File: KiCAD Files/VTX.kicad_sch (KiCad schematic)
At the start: 33 parts, among them J2 XT90PW-M, U1 LM76003RNPR, U2 LM76003RNPR

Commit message: USB Controller Ready
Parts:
- removed C1, C10: 470n, Footprints:C0805X474K101T, symbol C0805X474K101T:C0805X475K025T
- removed C11, C7: 1u, Footprints:CC0603KRX5R6BB105, symbol CL10A474KB8NNNC:CL10A474KB8NNNC
- removed C12, C2: 2.2uF, Footprints:CC0805KKX7R6BB225, symbol CC0805KKX7R6BB225:CC0805KKX7R6BB225
- removed C13, C3: 2.2uF, Footprints:CS1005X7R474K6R3NR, symbol CS1005X7R474K6R3NR:CC0805KKX7R6BB225
- removed C14, C6: 10p, Footprints:10pF16V, symbol 10pF16V:08051A100FAT2A
- removed C15, C8: 68u, Footprints:RR71C680MDN1, symbol RR71C680MDN1:RR71C680MDN1KX
- removed C16, C5: 470n, Footprints:CL10A474KB8NNNC, symbol CL10A474KB8NNNC:CL10A474KB8NNNC
- removed C4, C9: 4.7u, Footprints:CS3225X7R475K101NRK, symbol CS3225X7R475K101NRK:C1210C475K3PACTU
- removed L1, L2: 6060_78439346150, Footprints:L78439346150, symbol 78439346150:6060_78439346150
- removed R1, R5: 105K, Footprints:RC1206FR-07105KL, symbol RC1206FR-07105KL:RC1206FR-07105KL
- removed R2, R7: 24K9, Footprints:AC0402FR-0724K9L, symbol AC0402FR-0724K9L:AC0402FR-0724K9L
- removed R3, R4, R6, R8: 100K, Footprints:RC0402FR-07100KL, symbol RC0402FR-07100KL:RC0402FR-07100KL
- removed U1, U2: LM76003RNPR, Footprints:LM76003RNPR, symbol LM76003RNPR:LM76003RNPR
- added J1: Conn_02x20_Odd_Even, Connector_PinHeader_2.54mm:PinHeader_2x20_P2.54mm_Vertical, symbol Connector_Generic:Conn_02x20_Odd_Even
- added U1: BL-M8812EU2, Package_DFN_QFN:Texas_RVA_VQFN-16-1EP_3.5x3.5mm_P0.5mm_EP2.14x2.14mm_ThermalVias, symbol BL-M8812EU2:BL-M8812EU2
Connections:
- net GND: now also J1.14 (Pin_14), J1.20 (Pin_20), J1.25 (Pin_25), J1.30 (Pin_30), J1.34 (Pin_34), J1.39 (Pin_39), J1.6 (Pin_6), J1.9 (Pin_9), U1.1 (GND), U1.10 (GND), U1.11 (GND), U1.12 (GND), U1.13 (GND), U1.14 (GND), U1.15 (GND), U1.16 (GND), U1.17 (GND), U1.18 (GND), U1.19 (GND), U1.20 (GND), U1.21 (GND), U1.22 (GND), U1.23 (GND), U1.24 (GND), U1.25 (GND), U1.26 (GND), U1.27 (GND), U1.28 (GND), U1.29 (GND), U1.30 (GND), U1.31 (GND), U1.32 (GND), U1.33 (GND), U1.34 (GND), U1.35 (GND), U1.36 (GND), U1.37 (GND), U1.38 (GND), U1.4 (GND), U1.8 (GND), U1.9 (GND)
- new net +5V_Radxa: J1.2 (Pin_2), J1.4 (Pin_4)
- new net +5V_WiFi: U1.6 (VDD5.0), U1.7 (VDD5.0)
- new net USB Hub/USBDM_DN1: U1.3 (USB2.0-DM)
- new net USB Hub/USBDP_DN1: U1.2 (USB2.0+DP)
- new net USBDM_UP: J1.28 (Pin_28)
- new net USBDP_UP: J1.27 (Pin_27)
- no-connect marks 2 -> 1
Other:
- added sheet Buck Converter (buck_converter.kicad_sch)
- added sheet USB Hub (usb_hub.kicad_sch)
- note added: "BL-M8812EU2"
- note added: "Mounting Holes"
- note added: "Radxa ZERO 3W"
- note removed: "Buck Converter 1"
- note removed: "Buck Converter 2"
- moved on the sheet: H1, H2, H3, H4, J2

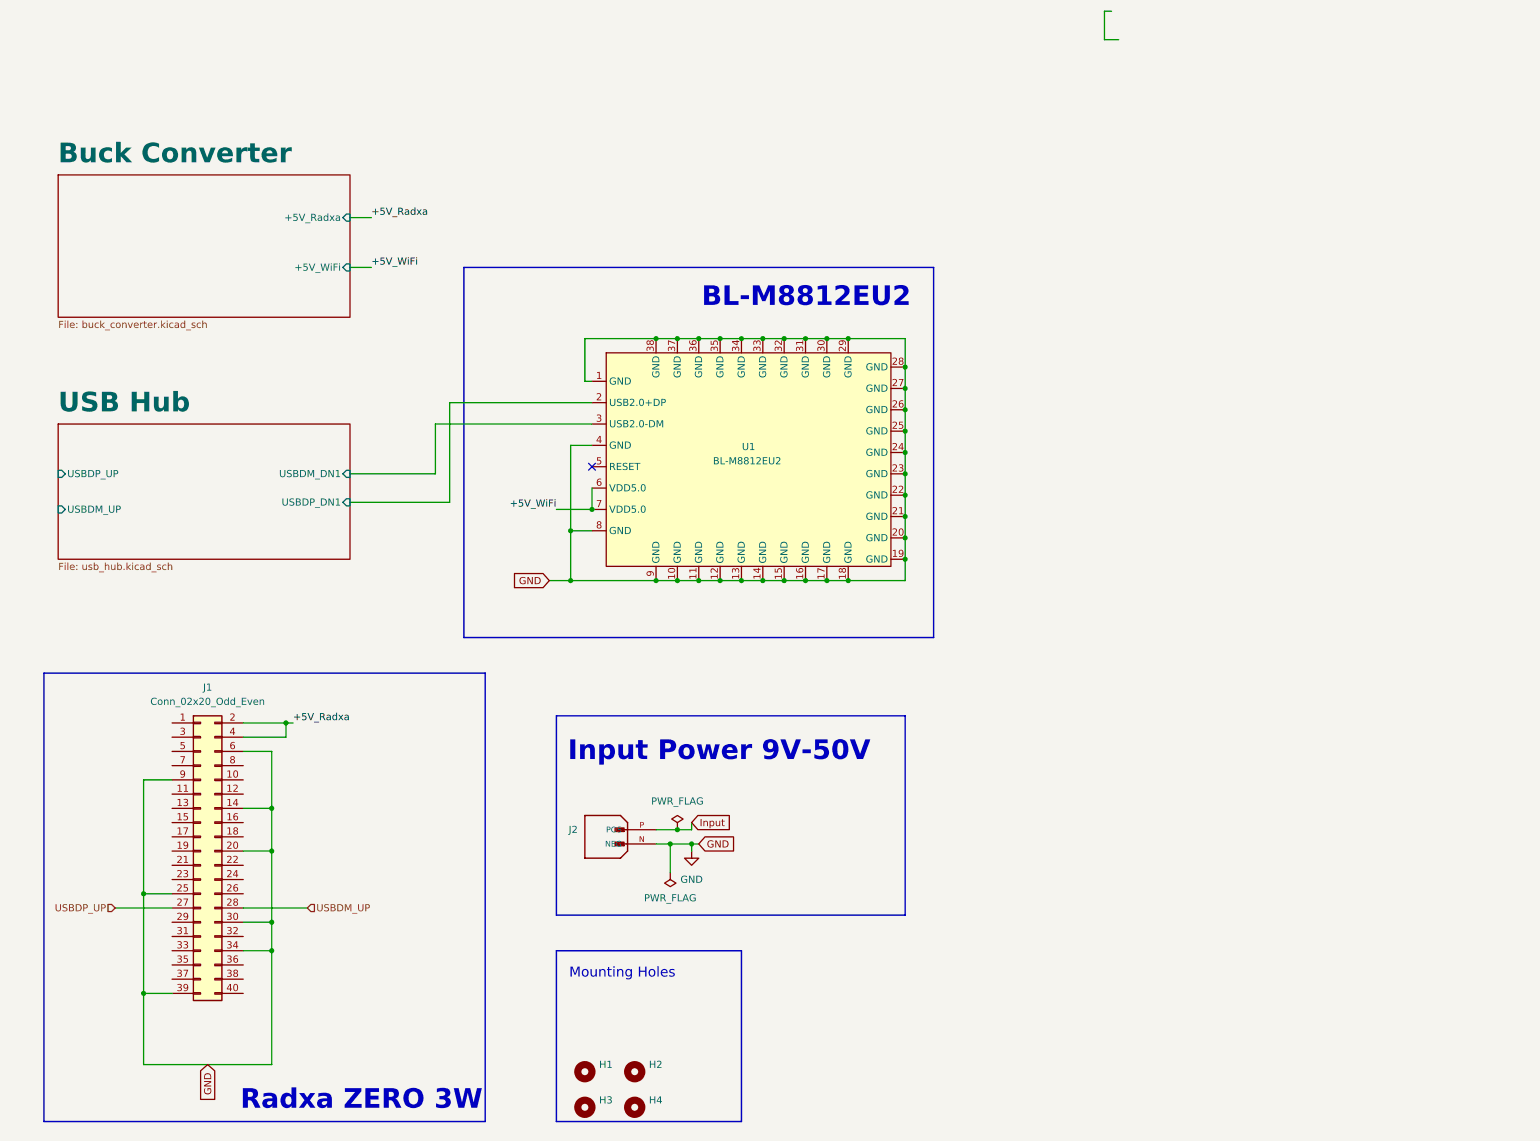
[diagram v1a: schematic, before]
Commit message: Ethernet routing pending
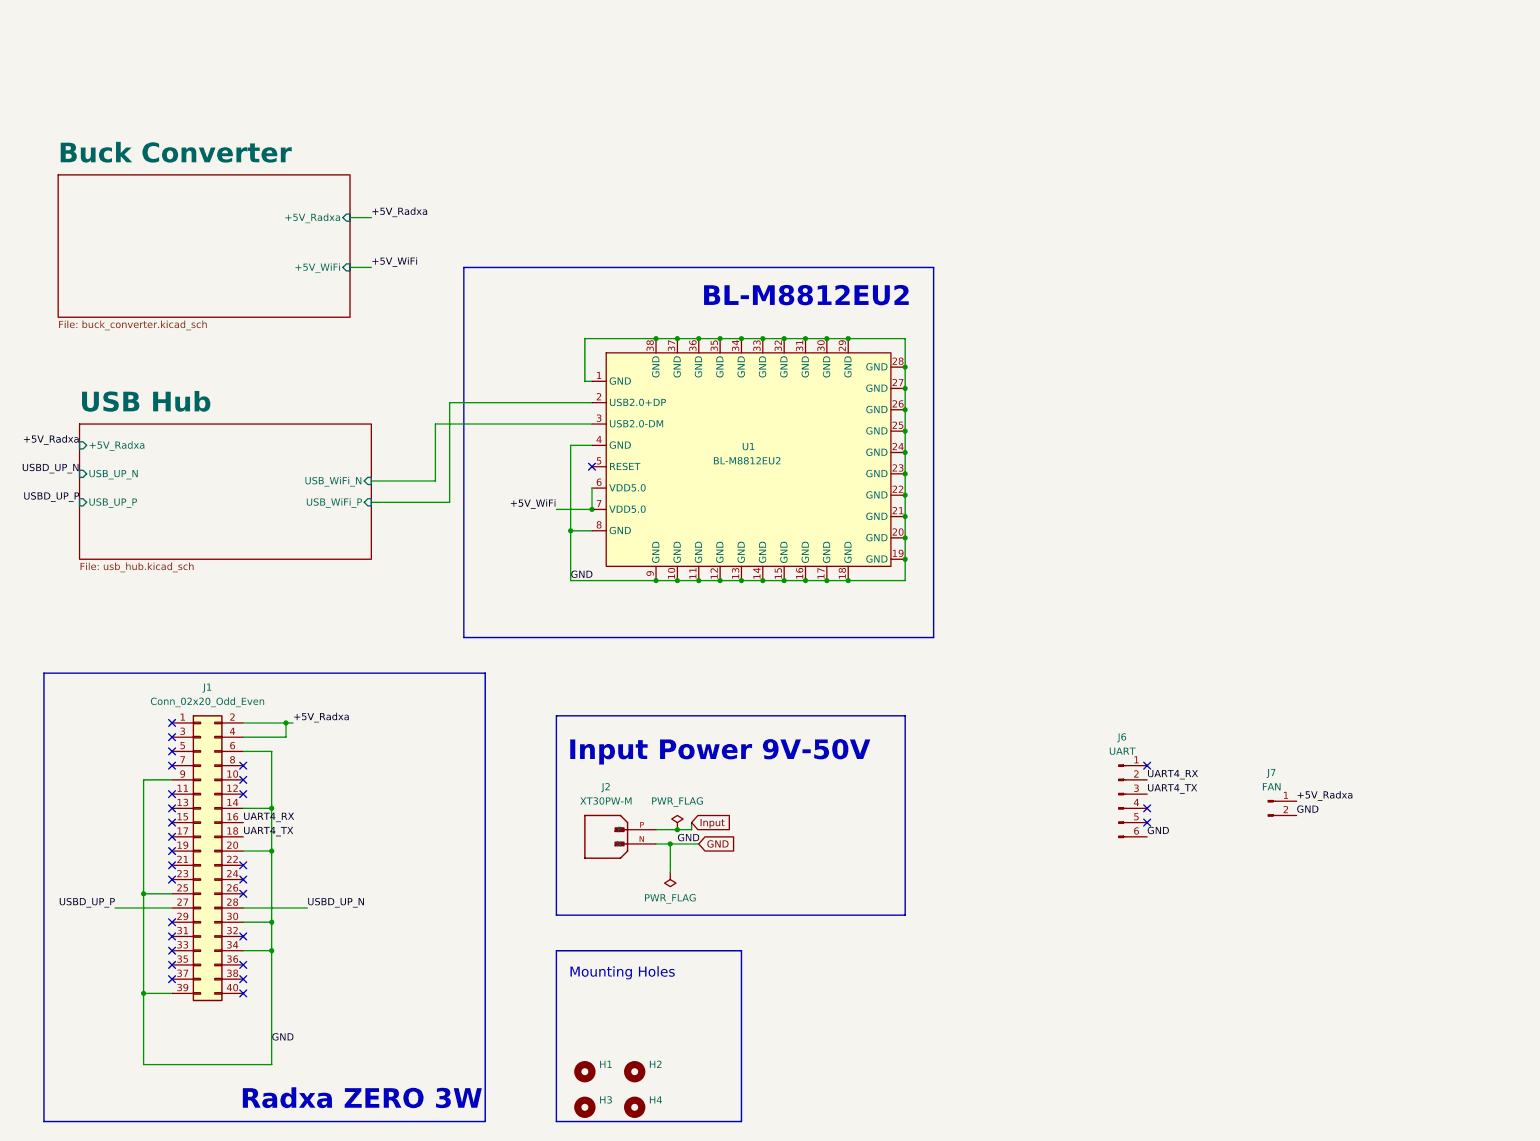
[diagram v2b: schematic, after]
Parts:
- removed J2: XT90PW-M, Footprints:AMASS_XT90PW-M, symbol XT90PW-M:XT90PW-M
- added J2: XT30PW-M, Footprints:AMASS_XT30PW-M, symbol XT30PW-M:XT30PW-M
- added J6: UART, Connector_JST:JST_GH_SM06B-GHS-TB_1x06-1MP_P1.25mm_Horizontal, symbol Connector:Conn_01x06_Pin
- added J7: FAN, Connector_JST:JST_GH_SM02B-GHS-TB_1x02-1MP_P1.25mm_Horizontal, symbol Connector:Conn_01x02_Pin
- U1: footprint Package_DFN_QFN:Texas_RVA_VQFN-16-1EP_3.5x3.5mm_P0.5mm_EP2.14x2.14mm_ThermalVias -> Footprints:BL-M8812EU2
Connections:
- net +5V_Radxa: now also J7.1 (Pin_1)
- net GND: now also J2.N, J6.6 (Pin_6), J7.2 (Pin_2)
- net Input: now also J2.P
- net UART4_RX: now reaches J1.16 (Pin_16)
- net UART4_RX: now also J6.2 (Pin_2)
- net UART4_TX: now reaches J1.18 (Pin_18)
- net UART4_TX: now also J6.3 (Pin_3)
- net USB Hub/USBDM_DN1 renamed USB Hub/USB_WiFi_N
- net USB Hub/USBDP_DN1 renamed USB Hub/USB_WiFi_P
- net USBDM_UP renamed USBD_UP_N
- net USBDP_UP renamed USBD_UP_P
- no-connect marks 1 -> 30
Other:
- sheet USB Hub ports: added +5V_Radxa, USB_UP_N, USB_UP_P, USB_WiFi_N, USB_WiFi_P; removed USBDM_DN1, USBDM_UP, USBDP_DN1, USBDP_UP
